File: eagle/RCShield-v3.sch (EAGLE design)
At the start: 52 parts, among them J1/J2 JOYSTICKPTH, P1/P3 POT, P2/P4 POT, Q1 MMBT3906, U1 TOUSCRUINO_SHIELD, U2 FT232RL-BASICSSOP, U4 XBEE, X1 USBSMD

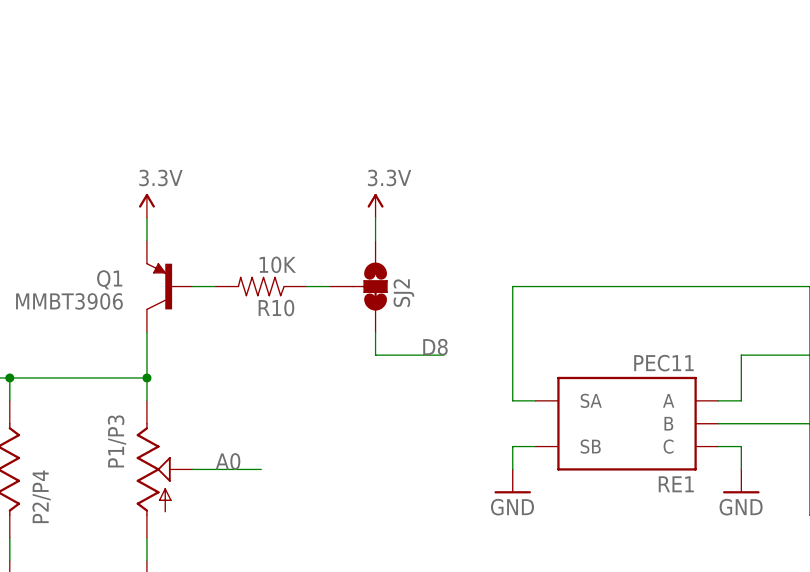
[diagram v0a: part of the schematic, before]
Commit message: 
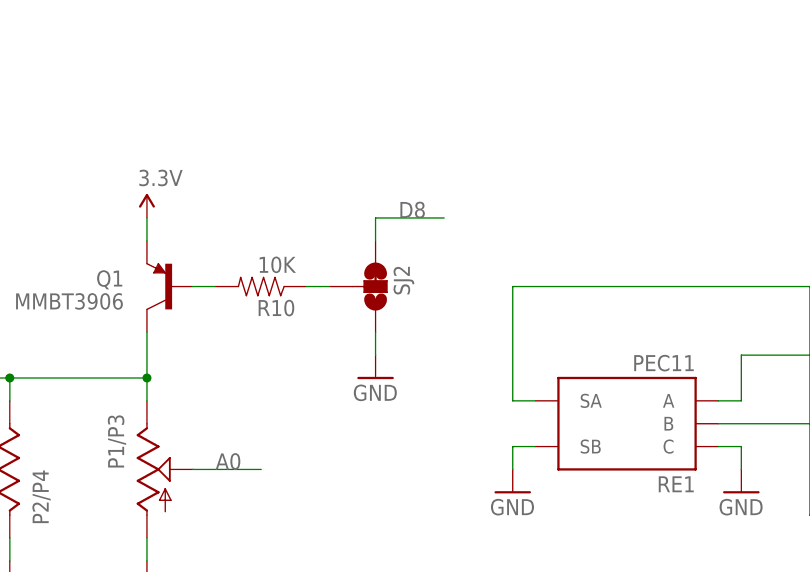
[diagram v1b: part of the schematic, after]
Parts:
- X1: value USBSMD -> USB-MICROB; device SparkFun:USBSMD -> SparkFun:USB-MICROB
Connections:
- net 3.3V: no longer SJ2.3
- net GND: now also SJ2.3
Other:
- moved on the sheet: SJ2
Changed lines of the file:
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@@
 <part name="U4" library="wibauxl" deviceset="XBEE-RSSI" device="" value="XBEE"/>
 <part name="J1/J2" library="SparkFun" deviceset="JOYSTICK" device="PTH"/>
-<part name="X1" library="SparkFun" deviceset="USB" device="SMD"/>
+<part name="X1" library="SparkFun" deviceset="USB" device="-MICROB" value="USB-MICROB"/>
 <part name="GND3" library="SparkFun" deviceset="GND" device=""/>
 <part name="C2" library="SparkFun" deviceset="CAP" device="0805" value="0.1uF"/>
@@
 <part name="SJ2" library="wibauxl" deviceset="SJ_2WAYS_1-2" device="W" value=""/>
 <part name="Q1" library="wibauxl" deviceset="TRANSISTOR_PNP" device="SMD" value="MMBT3906"/>
-<part name="P+16" library="SparkFun" deviceset="3.3V" device=""/>
 <part name="R10" library="SparkFun" deviceset="RESISTOR" device="0805-RES" value="10K"/>
 <part name="P+17" library="SparkFun" deviceset="3.3V" device=""/>
@@
 <part name="JP10" library="wibauxl" deviceset="M04" device="" value=""/>
 <part name="GND13" library="SparkFun" deviceset="GND" device=""/>
+<part name="GND16" library="SparkFun" deviceset="GND" device=""/>
 </parts>
 <sheets>
@@
 <instance part="JP2" gate="G$1" x="111.76" y="337.82"/>
 <instance part="JP3" gate="G$1" x="22.86" y="134.62"/>
-<instance part="SJ2" gate="G$1" x="127" y="162.56" rot="R180"/>
+<instance part="SJ2" gate="G$1" x="127" y="162.56" rot="MR0"/>
 <instance part="Q1" gate="G$1" x="104.14" y="162.56" rot="MR0"/>
-<instance part="P+16" gate="G$1" x="127" y="170.18"/>
 <instance part="R10" gate="G$1" x="114.3" y="162.56" rot="R180"/>
 <instance part="P+17" gate="G$1" x="101.6" y="170.18"/>
@@
 <instance part="JP10" gate="G$1" x="86.36" y="101.6" rot="MR0"/>
 <instance part="GND13" gate="1" x="78.74" y="93.98" rot="MR0"/>
+<instance part="GND16" gate="1" x="127" y="152.4"/>
 </instances>
 <busses>
@@
 <pinref part="GND13" gate="1" pin="GND"/>
 </segment>
+<segment>
+<pinref part="SJ2" gate="G$1" pin="3"/>
+<wire x1="127" y1="157.48" x2="127" y2="154.94" width="0.1524" layer="91"/>
+<pinref part="GND16" gate="1" pin="GND"/>
+</segment>
 </net>
 <net name="3.3V" class="0">
@@
 <pinref part="U2" gate="G$1" pin="VCCIO"/>
 <pinref part="P+15" gate="G$1" pin="3.3V"/>
-</segment>
-<segment>
-<pinref part="P+16" gate="G$1" pin="3.3V"/>
-<pinref part="SJ2" gate="G$1" pin="3"/>
-<wire x1="127" y1="170.18" x2="127" y2="167.64" width="0.1524" layer="91"/>
 </segment>
 <segment>
@@
 <segment>
 <pinref part="SJ2" gate="G$1" pin="1"/>
-<wire x1="127" y1="157.48" x2="127" y2="154.94" width="0.1524" layer="91"/>
-<wire x1="127" y1="154.94" x2="134.62" y2="154.94" width="0.1524" layer="91"/>
-<label x="132.08" y="154.94" size="1.778" layer="95"/>
+<wire x1="127" y1="167.64" x2="127" y2="170.18" width="0.1524" layer="91"/>
+<wire x1="127" y1="170.18" x2="134.62" y2="170.18" width="0.1524" layer="91"/>
+<label x="129.54" y="170.18" size="1.778" layer="95"/>
 </segment>
 </net>
@@
 <pinref part="R10" gate="G$1" pin="2"/>
 <wire x1="106.68" y1="162.56" x2="109.22" y2="162.56" width="0.1524" layer="91"/>
-</segment>
-</net>
-<net name="N$3" class="0">
-<segment>
-<pinref part="R10" gate="G$1" pin="1"/>
-<pinref part="SJ2" gate="G$1" pin="2"/>
-<wire x1="119.38" y1="162.56" x2="121.92" y2="162.56" width="0.1524" layer="91"/>
 </segment>
 </net>
@@
 </segment>
 </net>
+<net name="N$3" class="0">
+<segment>
+<pinref part="R10" gate="G$1" pin="1"/>
+<pinref part="SJ2" gate="G$1" pin="2"/>
+<wire x1="119.38" y1="162.56" x2="121.92" y2="162.56" width="0.1524" layer="91"/>
+</segment>
+</net>

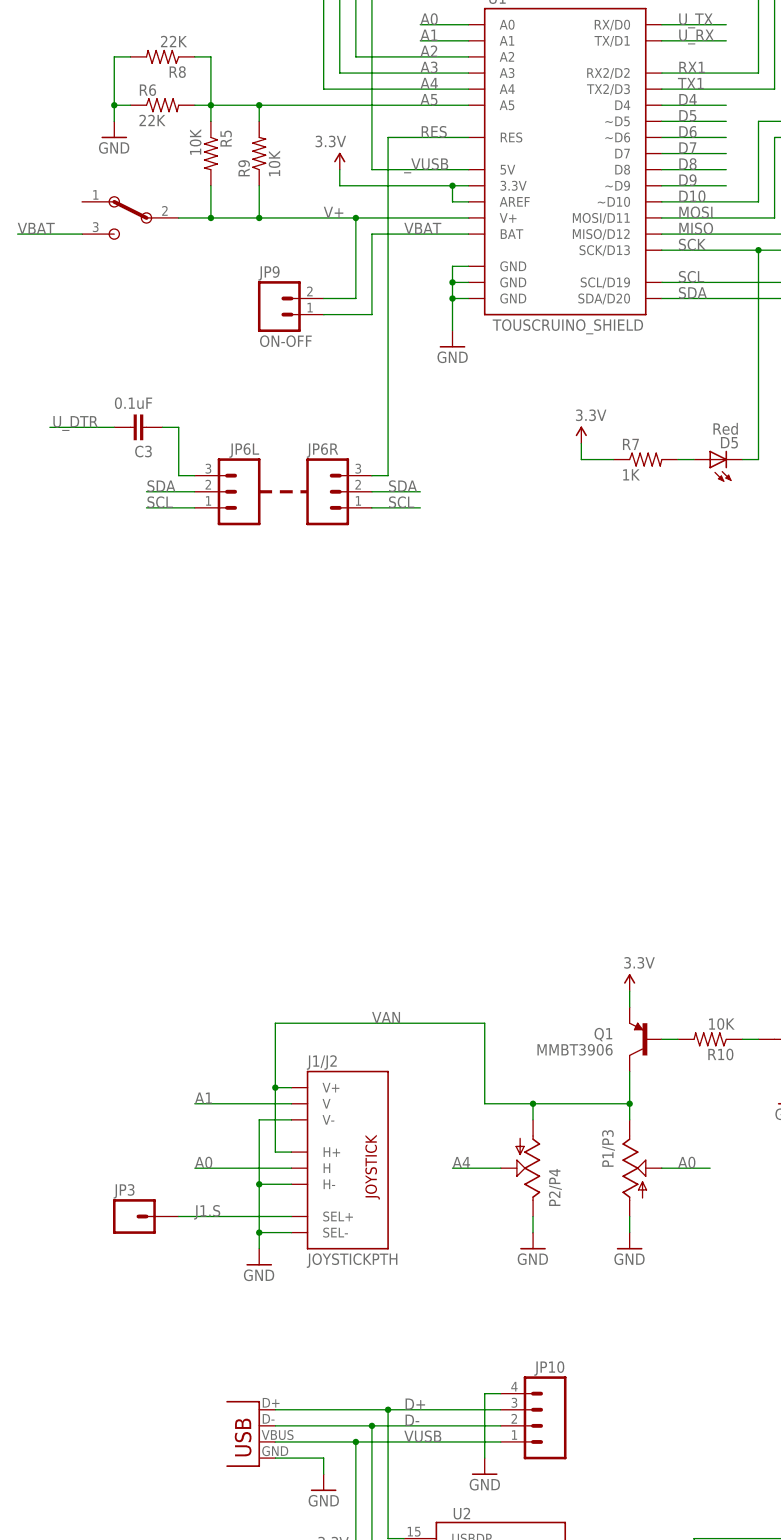
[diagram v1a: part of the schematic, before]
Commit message: 
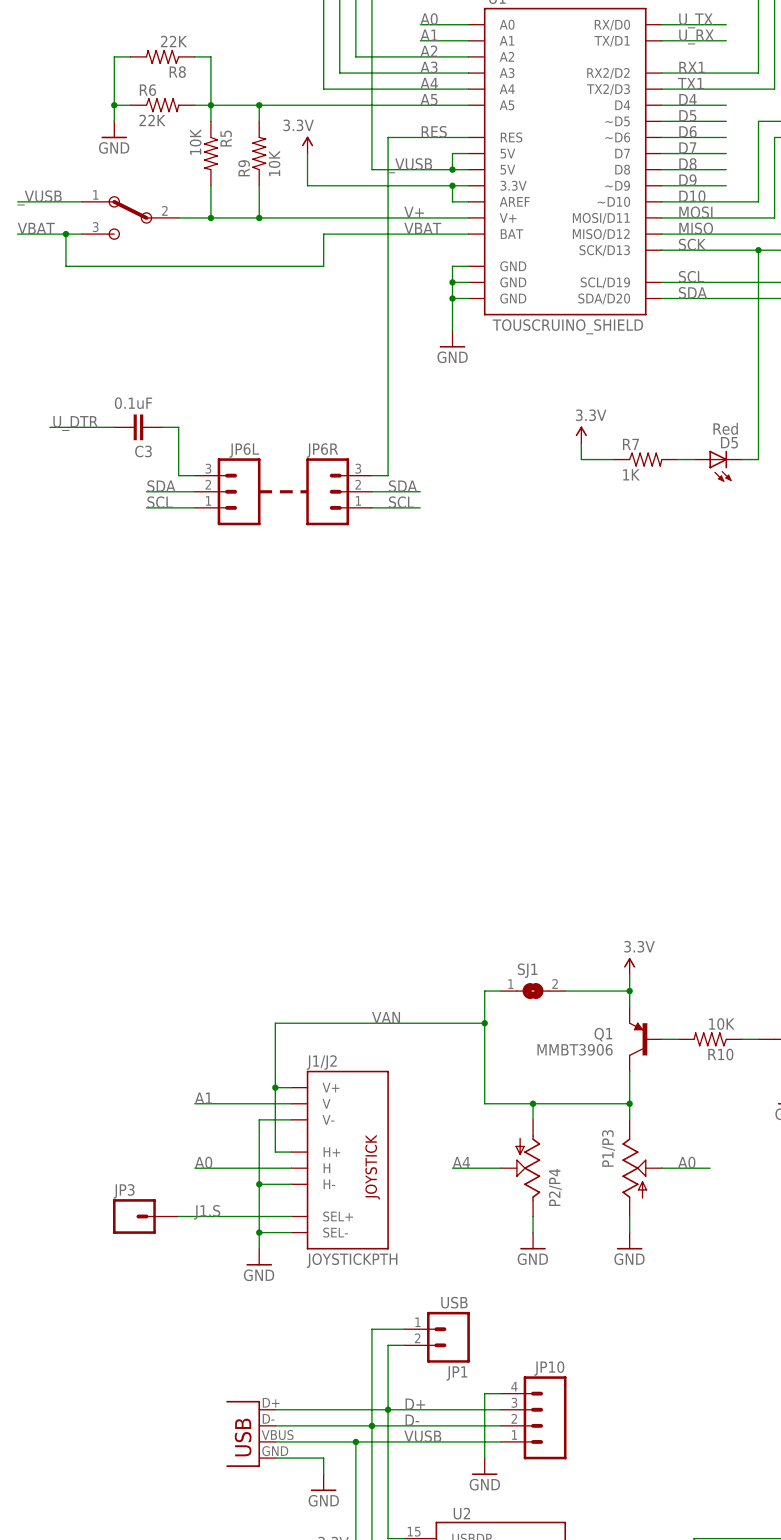
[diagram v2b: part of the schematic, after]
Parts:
- removed JP9: ON-OFF, wibauxl:M02
- added JP1: USB, wibauxl:M02
- added SJ1: (no value), wibauxl:SJ
- X1: value USB-MICROB -> USB; device SparkFun:USB-MICROB -> wibauxl:USB
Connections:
- net 3.3V: now also SJ1.2
- net D+: now also JP1.2
- net D-: now also JP1.1
- net V+: no longer JP9.2
- net VAN: now also SJ1.1
- net VBAT: no longer JP9.1
- net _VUSB: now also S4.1, U1.5V@0, U1.5V@1; no longer U1.5V
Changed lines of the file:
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@@
 <part name="U4" library="wibauxl" deviceset="XBEE-RSSI" device="" value="XBEE"/>
 <part name="J1/J2" library="SparkFun" deviceset="JOYSTICK" device="PTH"/>
-<part name="X1" library="SparkFun" deviceset="USB" device="-MICROB" value="USB-MICROB"/>
+<part name="X1" library="wibauxl" deviceset="USB" device="" value="USB"/>
 <part name="GND3" library="SparkFun" deviceset="GND" device=""/>
 <part name="C2" library="SparkFun" deviceset="CAP" device="0805" value="0.1uF"/>
@@
 <part name="P+14" library="SparkFun" deviceset="3.3V" device=""/>
 <part name="R7" library="SparkFun" deviceset="RESISTOR" device="0805-RES" value="1K"/>
-<part name="JP9" library="wibauxl" deviceset="M02" device="" value="ON-OFF"/>
 <part name="SJ3" library="jumper" deviceset="SJ" device=""/>
 <part name="C3" library="SparkFun" deviceset="CAP" device="0805" value="0.1uF"/>
@@
 <part name="GND13" library="SparkFun" deviceset="GND" device=""/>
 <part name="GND16" library="SparkFun" deviceset="GND" device=""/>
+<part name="JP1" library="wibauxl" deviceset="M02" device="" value="USB"/>
+<part name="SJ1" library="wibauxl" deviceset="SJ" device=""/>
 </parts>
 <sheets>
@@
 <instance part="P+1" gate="G$1" x="134.62" y="88.9"/>
 <instance part="U1" gate="G$1" x="91.44" y="302.26"/>
-<instance part="P+2" gate="G$1" x="55.88" y="299.72" rot="MR0"/>
+<instance part="P+2" gate="G$1" x="50.8" y="302.26" rot="MR0"/>
 <instance part="GND1" gate="1" x="73.66" y="271.78" rot="MR0"/>
 <instance part="P+3" gate="G$1" x="10.16" y="350.52" rot="MR0"/>
@@
 <instance part="P+14" gate="G$1" x="93.98" y="256.54"/>
 <instance part="R7" gate="G$1" x="104.14" y="254"/>
-<instance part="JP9" gate="G$1" x="48.26" y="276.86"/>
 <instance part="SJ3" gate="1" x="198.12" y="147.32"/>
 <instance part="C3" gate="G$1" x="25.4" y="259.08" smashed="yes" rot="MR270">
@@
 <instance part="Q1" gate="G$1" x="104.14" y="162.56" rot="MR0"/>
 <instance part="R10" gate="G$1" x="114.3" y="162.56" rot="R180"/>
-<instance part="P+17" gate="G$1" x="101.6" y="170.18"/>
+<instance part="P+17" gate="G$1" x="101.6" y="172.72"/>
 <instance part="JP7" gate="G$1" x="147.32" y="266.7" rot="MR0"/>
 <instance part="JP4" gate="G$1" x="182.88" y="261.62" rot="MR0"/>
@@
 <instance part="GND13" gate="1" x="78.74" y="93.98" rot="MR0"/>
 <instance part="GND16" gate="1" x="127" y="152.4"/>
+<instance part="JP1" gate="G$1" x="71.12" y="116.84" rot="R180"/>
+<instance part="SJ1" gate="1" x="86.36" y="170.18"/>
 </instances>
 <busses>
@@
 <segment>
 <wire x1="76.2" y1="297.18" x2="73.66" y2="297.18" width="0.1524" layer="91"/>
-<wire x1="73.66" y1="297.18" x2="55.88" y2="297.18" width="0.1524" layer="91"/>
-<wire x1="55.88" y1="297.18" x2="55.88" y2="299.72" width="0.1524" layer="91"/>
+<wire x1="73.66" y1="297.18" x2="50.8" y2="297.18" width="0.1524" layer="91"/>
+<wire x1="50.8" y1="297.18" x2="50.8" y2="302.26" width="0.1524" layer="91"/>
 <pinref part="U1" gate="G$1" pin="3.3V"/>
 <pinref part="P+2" gate="G$1" pin="3.3V"/>
@@
 <pinref part="P+17" gate="G$1" pin="3.3V"/>
 <pinref part="Q1" gate="G$1" pin="E"/>
+<wire x1="101.6" y1="172.72" x2="101.6" y2="170.18" width="0.1524" layer="91"/>
+<pinref part="SJ1" gate="1" pin="2"/>
 <wire x1="101.6" y1="170.18" x2="101.6" y2="167.64" width="0.1524" layer="91"/>
+<wire x1="91.44" y1="170.18" x2="101.6" y2="170.18" width="0.1524" layer="91"/>
+<junction x="101.6" y="170.18"/>
 </segment>
 <segment>
@@
 <wire x1="30.48" y1="292.1" x2="35.56" y2="292.1" width="0.1524" layer="91"/>
 <wire x1="35.56" y1="292.1" x2="43.18" y2="292.1" width="0.1524" layer="91"/>
-<wire x1="43.18" y1="292.1" x2="58.42" y2="292.1" width="0.1524" layer="91"/>
 <wire x1="35.56" y1="297.18" x2="35.56" y2="292.1" width="0.1524" layer="91"/>
-<wire x1="53.34" y1="279.4" x2="58.42" y2="279.4" width="0.1524" layer="91"/>
-<wire x1="58.42" y1="279.4" x2="58.42" y2="292.1" width="0.1524" layer="91"/>
 <wire x1="43.18" y1="297.18" x2="43.18" y2="292.1" width="0.1524" layer="91"/>
 <junction x="35.56" y="292.1"/>
-<junction x="58.42" y="292.1"/>
 <junction x="43.18" y="292.1"/>
 <pinref part="S4" gate="G$1" pin="2"/>
 <pinref part="R5" gate="G$1" pin="2"/>
-<pinref part="JP9" gate="G$1" pin="2"/>
 <pinref part="R9" gate="G$1" pin="1"/>
-<label x="53.34" y="292.1" size="1.778" layer="95"/>
+<label x="66.04" y="292.1" size="1.778" layer="95"/>
 <pinref part="U1" gate="G$1" pin="V+"/>
-<wire x1="58.42" y1="292.1" x2="76.2" y2="292.1" width="0.1524" layer="91"/>
+<wire x1="43.18" y1="292.1" x2="76.2" y2="292.1" width="0.1524" layer="91"/>
 </segment>
 </net>
 <net name="VBAT" class="0">
 <segment>
-<wire x1="76.2" y1="289.56" x2="60.96" y2="289.56" width="0.1524" layer="91"/>
-<wire x1="60.96" y1="289.56" x2="60.96" y2="276.86" width="0.1524" layer="91"/>
-<wire x1="60.96" y1="276.86" x2="53.34" y2="276.86" width="0.1524" layer="91"/>
+<wire x1="15.24" y1="289.56" x2="12.7" y2="289.56" width="0.1524" layer="91"/>
+<label x="5.08" y="289.56" size="1.778" layer="95"/>
+<pinref part="S4" gate="G$1" pin="3"/>
+<wire x1="12.7" y1="289.56" x2="5.08" y2="289.56" width="0.1524" layer="91"/>
+<wire x1="12.7" y1="289.56" x2="12.7" y2="284.48" width="0.1524" layer="91"/>
+<wire x1="12.7" y1="284.48" x2="53.34" y2="284.48" width="0.1524" layer="91"/>
+<wire x1="53.34" y1="284.48" x2="53.34" y2="289.56" width="0.1524" layer="91"/>
+<wire x1="76.2" y1="289.56" x2="53.34" y2="289.56" width="0.1524" layer="91"/>
 <label x="66.04" y="289.56" size="1.778" layer="95"/>
 <pinref part="U1" gate="G$1" pin="BAT"/>
-<pinref part="JP9" gate="G$1" pin="1"/>
-</segment>
-<segment>
-<wire x1="15.24" y1="289.56" x2="5.08" y2="289.56" width="0.1524" layer="91"/>
-<label x="5.08" y="289.56" size="1.778" layer="95"/>
-<pinref part="S4" gate="G$1" pin="3"/>
+<junction x="12.7" y="289.56"/>
 </segment>
 </net>
@@
 <segment>
 <wire x1="50.8" y1="345.44" x2="60.96" y2="345.44" width="0.1524" layer="91"/>
-<wire x1="76.2" y1="299.72" x2="60.96" y2="299.72" width="0.1524" layer="91"/>
+<wire x1="76.2" y1="299.72" x2="73.66" y2="299.72" width="0.1524" layer="91"/>
+<wire x1="73.66" y1="299.72" x2="60.96" y2="299.72" width="0.1524" layer="91"/>
 <wire x1="60.96" y1="345.44" x2="60.96" y2="299.72" width="0.1524" layer="91"/>
-<label x="66.04" y="299.72" size="1.778" layer="95"/>
+<label x="63.5" y="299.72" size="1.778" layer="95"/>
 <pinref part="JP2R" gate="G$1" pin="5"/>
-<pinref part="U1" gate="G$1" pin="5V"/>
+<pinref part="U1" gate="G$1" pin="5V@0"/>
+<pinref part="U1" gate="G$1" pin="5V@1"/>
+<wire x1="76.2" y1="302.26" x2="73.66" y2="302.26" width="0.1524" layer="91"/>
+<wire x1="73.66" y1="302.26" x2="73.66" y2="299.72" width="0.1524" layer="91"/>
+<junction x="73.66" y="299.72"/>
+</segment>
+<segment>
+<pinref part="S4" gate="G$1" pin="1"/>
+<wire x1="15.24" y1="294.64" x2="5.08" y2="294.64" width="0.1524" layer="91"/>
+<label x="5.08" y="294.64" size="1.778" layer="95"/>
 </segment>
 </net>
@@
 <junction x="63.5" y="104.14"/>
 <pinref part="JP10" gate="G$1" pin="3"/>
+<wire x1="63.5" y1="104.14" x2="63.5" y2="114.3" width="0.1524" layer="91"/>
+<pinref part="JP1" gate="G$1" pin="2"/>
+<wire x1="63.5" y1="114.3" x2="66.04" y2="114.3" width="0.1524" layer="91"/>
 </segment>
 </net>
@@
 <junction x="60.96" y="101.6"/>
 <pinref part="JP10" gate="G$1" pin="2"/>
+<wire x1="60.96" y1="101.6" x2="60.96" y2="116.84" width="0.1524" layer="91"/>
+<pinref part="JP1" gate="G$1" pin="1"/>
+<wire x1="60.96" y1="116.84" x2="66.04" y2="116.84" width="0.1524" layer="91"/>
 </segment>
 </net>
@@
 <junction x="86.36" y="152.4"/>
 <label x="60.96" y="165.1" size="1.778" layer="95"/>
-</segment>
-<segment>
+<wire x1="78.74" y1="165.1" x2="78.74" y2="170.18" width="0.1524" layer="91"/>
+<pinref part="SJ1" gate="1" pin="1"/>
+<wire x1="78.74" y1="170.18" x2="81.28" y2="170.18" width="0.1524" layer="91"/>
+<junction x="78.74" y="165.1"/>
+</segment>
+<segment>
